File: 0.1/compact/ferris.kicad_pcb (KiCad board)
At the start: 2 copper layers, 208.7 x 86.7 mm, 102 parts, among them J1 USB C, K0_0 KEYSW, K0_1 KEYSW, K0_2 KEYSW, K0_3 KEYSW, K0_4 KEYSW, K0_5 KEYSW, K0_6 KEYSW, K0_7 KEYSW, K0_8 KEYSW, K0_9 KEYSW, K1_0 KEYSW, K1_1 KEYSW, K1_2 KEYSW, K1_3 KEYSW, K1_4 KEYSW, K1_5 KEYSW, K1_6 KEYSW, K1_7 KEYSW, K1_8 KEYSW, K1_9 KEYSW, K2_0 KEYSW, K2_1 KEYSW, K2_2 KEYSW, K2_3 KEYSW, K2_4 KEYSW, K2_5 KEYSW, K2_6 KEYSW, K2_7 KEYSW, K2_8 KEYSW, K2_9 KEYSW, K3_3 KEYSW, K3_4 KEYSW, K3_5 KEYSW, K3_6 KEYSW, SW1 SW_PUSH, U1 ATmega32U4-AU, U2 MCP23017_SO, Y1 Crystal

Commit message: Modify the switch footprint to add pad clearance.
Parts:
- K0_0, K0_1, K0_2, K0_3, K0_4, K0_5, K0_6, K0_7, K0_8, K0_9, K1_0, K1_1, K1_2, K1_3, K1_4, K1_5, K1_6, K1_7, K1_8, K1_9, K2_0, K2_1, K2_2, K2_3, K2_4, K2_5, K2_6, K2_7, K2_8, K2_9, K3_3, K3_4, K3_5, K3_6: footprint switches:Choc_PG1350_Choc_Spacing -> switches:Choc_PG1350_Choc_Spacing_with_jlcpb_safe_pad_clearance

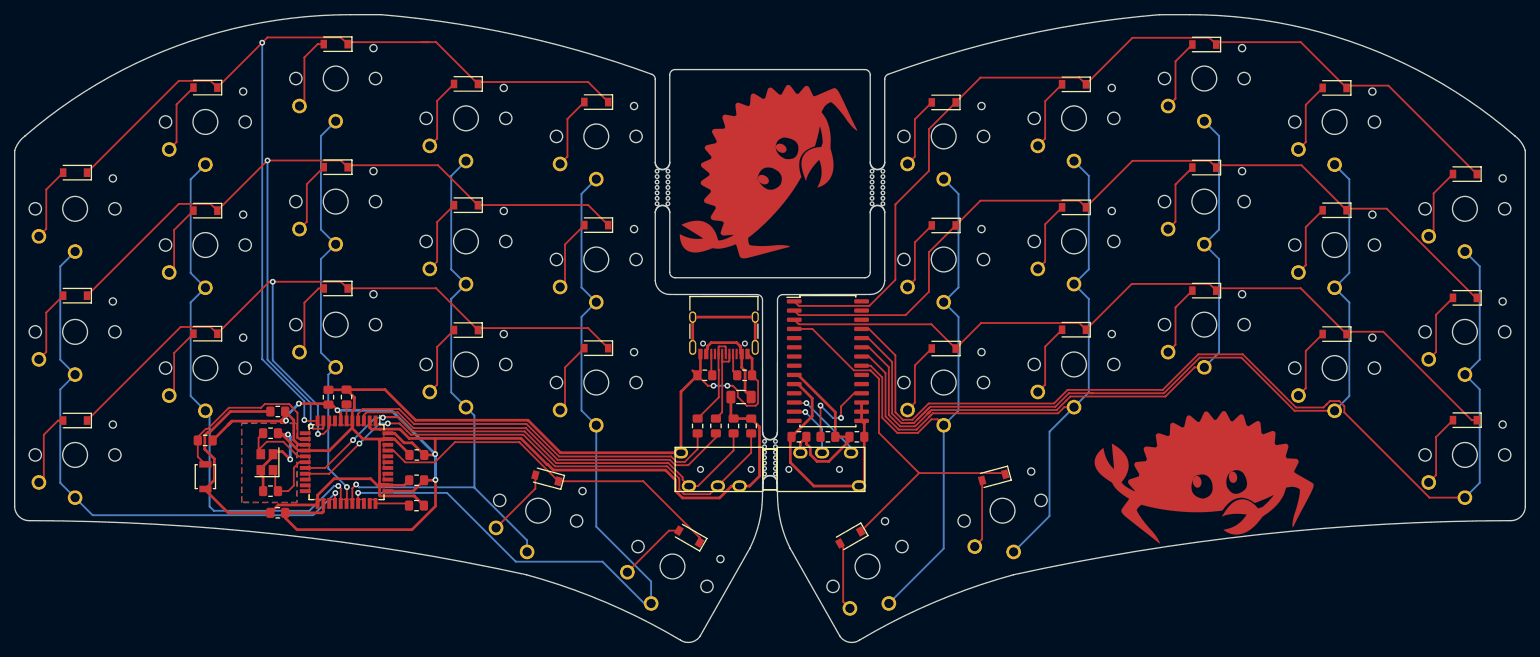
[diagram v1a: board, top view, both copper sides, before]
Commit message: Move traces around the jlcpcb clearance switch pads.
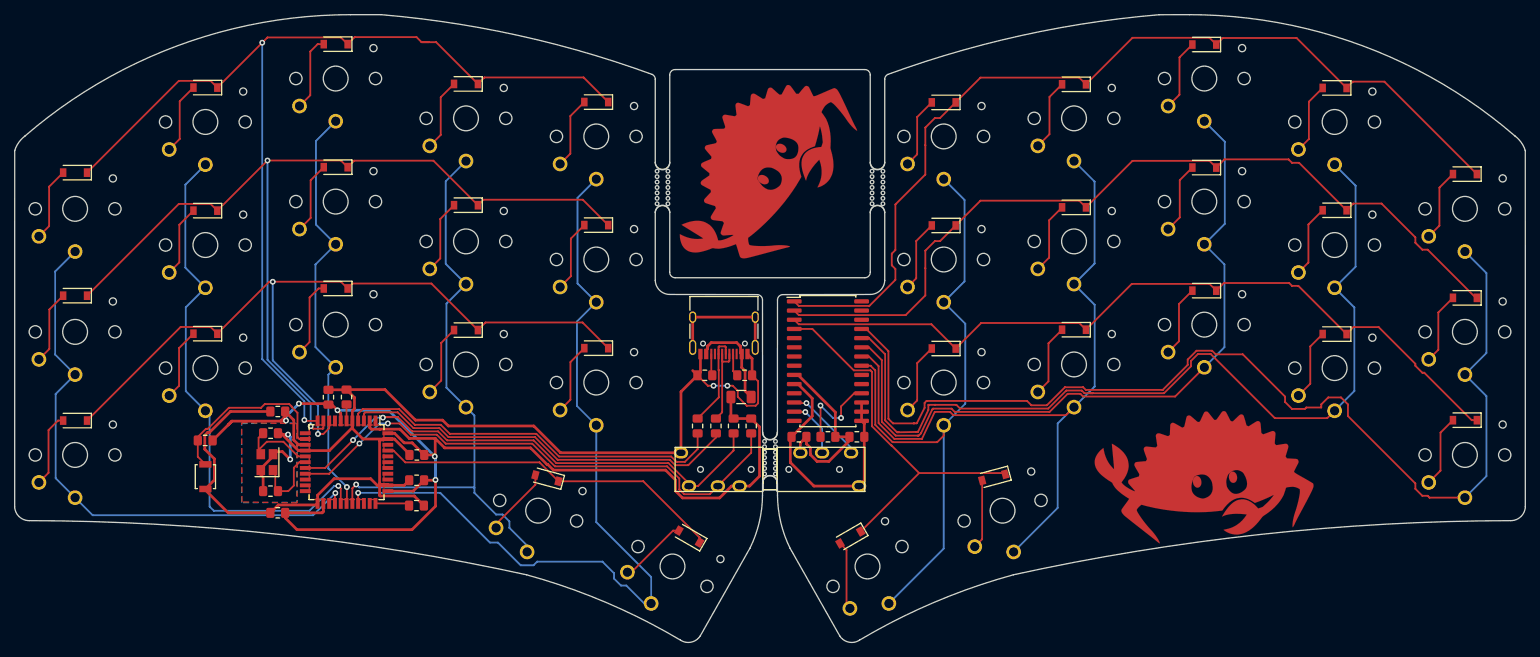
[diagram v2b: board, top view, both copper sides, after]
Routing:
- net /col9: track 143.7 -> 151.2 mm
- net /col6: track 99.5 -> 103.8 mm
- net /col8: track 121.9 -> 125.9 mm
- net /col7: track 97.4 -> 101.3 mm
- net /col5: track 84.7 -> 88.6 mm
- net /row0,3: track 51.1 -> 48.7 mm
- net /row1,1: track 115.6 -> 117.8 mm
- net /col4: track 113.4 -> 115.2 mm
- net /row1,0: track 128.5 -> 130.2 mm
- net /col3: track 80.2 -> 81.9 mm
- net /row1,2: track 108.7 -> 110.0 mm
- net /col2: track 57.7 -> 58.9 mm
- net /row0,2: track 111.3 -> 112.4 mm
- net /col1: track 72.9 -> 74.0 mm
- net /col0: track 77.1 -> 78.2 mm
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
